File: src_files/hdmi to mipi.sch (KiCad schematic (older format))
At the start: 37 parts, among them J1 HDMI-019S, J7 XF2M60151AH, U9 TC358870XBG_NOK_, Y3 CRYSTAL_48MHZ

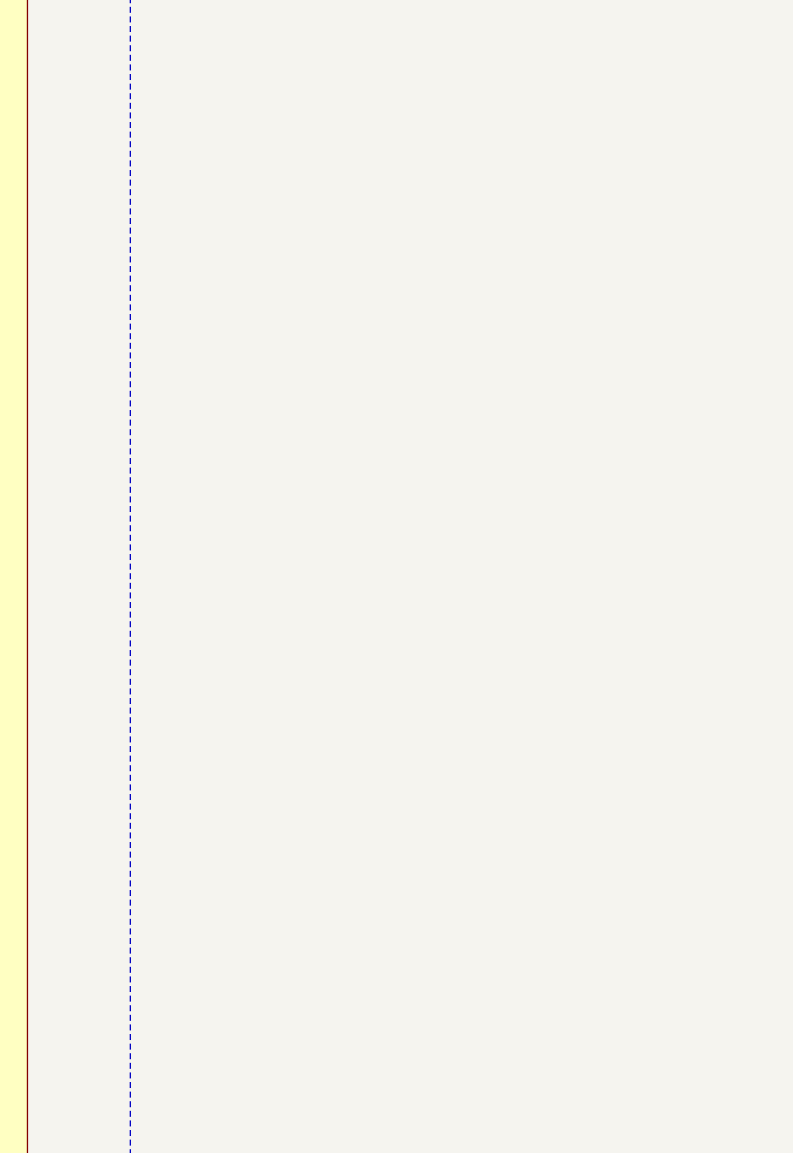
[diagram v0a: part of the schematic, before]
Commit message: update 1 extra hdmi to mipi interface
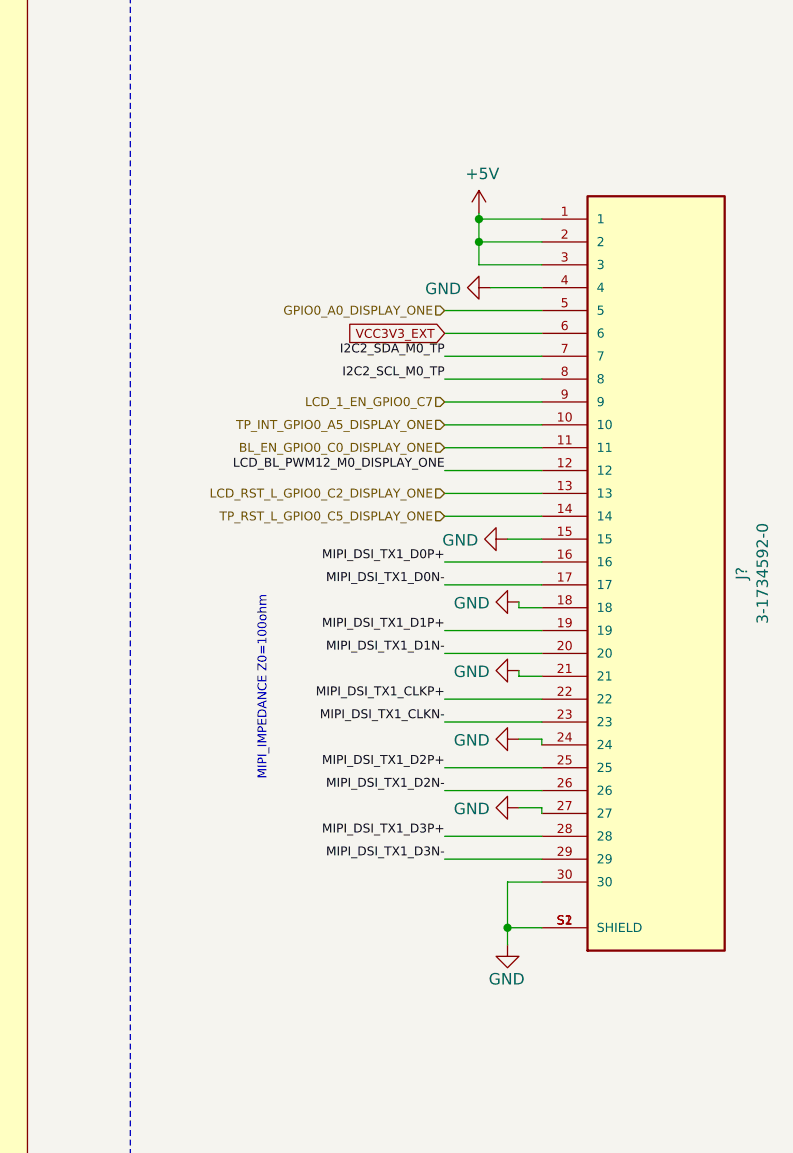
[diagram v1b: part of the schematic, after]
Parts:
- added J?: 3-1734592-0, greencharge-footprints:TE_3-1734592-0, symbol 3-1734592-0:3-1734592-0
- U9: value TC358870XBG_NOK_ -> TC358870XBG_NOK_
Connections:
- net GND: now also J?.15, J?.18, J?.21, J?.24, J?.27, J?.30, J?.4, J?.S1 (SHIELD), J?.S2 (SHIELD)
- new net +5V: J?.1, J?.2, J?.3
- new net BL_EN_GPIO0_C0_DISPLAY_ONE: J?.11
- new net GPIO0_A0_DISPLAY_ONE: J?.5
- new net I2C2_SCL_M0_TP: J?.8
- new net I2C2_SDA_M0_TP: J?.7
- new net LCD_1_EN_GPIO0_C7: J?.9
- new net LCD_BL_PWM12_M0_DISPLAY_ONE: J?.12
- new net LCD_RST_L_GPIO0_C2_DISPLAY_ONE: J?.13
- new net MIPI_DSI_TX1_CLKN-: J?.23
- new net MIPI_DSI_TX1_CLKP+: J?.22
- new net MIPI_DSI_TX1_D0N-: J?.17
- new net MIPI_DSI_TX1_D0P+: J?.16
- new net MIPI_DSI_TX1_D1N-: J?.20
- new net MIPI_DSI_TX1_D1P+: J?.19
- new net MIPI_DSI_TX1_D2N-: J?.26
- new net MIPI_DSI_TX1_D2P+: J?.25
- new net MIPI_DSI_TX1_D3N-: J?.29
- new net MIPI_DSI_TX1_D3P+: J?.28
- new net TP_INT_GPIO0_A5_DISPLAY_ONE: J?.10
- new net TP_RST_L_GPIO0_C5_DISPLAY_ONE: J?.14
- new net VCC3V3_EXT: J?.6
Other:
- note added: "MIPI_IMPEDANCE Z0=100ohm"
